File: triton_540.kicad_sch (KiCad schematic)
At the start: 24 parts, among them J1 REC ANT, SW1 Band Switch B

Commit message: first draft of vfo sheet
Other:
- added sheet VFO-80289 (VFO_80289.kicad_sch)
- note added: "VFO 80289"
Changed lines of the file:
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@@
 		(title "Ten Tec Triton IV Model 540 Transceiver")
 		(date "2026-07-26")
-		(rev "0.1")
+		(rev "0.2")
 		(company "Andy McCann KA3KAF & DOug McCann KA3KAG")
 	)
@@
 		)
 	)
+	(text "VFO\n80289"
+		(exclude_from_sim no)
+		(at 166.116 122.174 0)
+		(effects
+			(font
+				(size 2.54 2.54)
+			)
+		)
+	)
 	(junction
 		(at 123.19 80.01)
@@
 				)
 			)
+		)
+	)
+	(sheet
+		(at 146.05 110.49)
+		(size 40.64 22.86)
+		(exclude_from_sim no)
+		(in_bom yes)
+		(on_board yes)
+		(dnp no)
+		(fields_autoplaced yes)
+		(stroke
+			(width 0.1524)
+			(type solid)
+		)
+		(fill
+			(color 0 0 0 0)
+		)
+		(property "Sheetname" "VFO-80289"
+			(at 146.05 109.7784 0)
+			(hide yes)
+			(show_name no)
+			(do_not_autoplace no)
+			(effects
+				(font
+					(size 1.27 1.27)
+				)
+				(justify left bottom)
+			)
+		)
+		(property "Sheetfile" "VFO_80289.kicad_sch"
+			(at 146.05 133.9346 0)
+			(hide yes)
+			(show_name no)
+			(do_not_autoplace no)
+			(effects
+				(font
+					(size 1.27 1.27)
+				)
+				(justify left top)
+			)
+		)
+		(pin "+12" input
+			(at 151.13 110.49 90)
+			(effects
+				(font
+					(size 1.27 1.27)
+				)
+				(justify right)
+			)
+		)
+		(pin "+REG" input
+			(at 166.37 110.49 90)
+			(effects
+				(font
+					(size 1.27 1.27)
+				)
+				(justify right)
+			)
+		)
+		(pin "OFFSET" input
+			(at 179.07 133.35 270)
+			(effects
+				(font
+					(size 1.27 1.27)
+				)
+				(justify left)
+			)
+		)
+		(pin "OUT" input
+			(at 186.69 115.57 0)
+			(effects
+				(font
+					(size 1.27 1.27)
+				)
+				(justify right)
+			)
+		)
+		(pin "S5" input
+			(at 166.37 133.35 270)
+			(effects
+				(font
+					(size 1.27 1.27)
+				)
+				(justify left)
+			)
+		)
+		(instances
+			(project "triton_540"
+				(path "/2d45daab-5f60-4e97-8c02-32b0054eab28"
+					(page "3")
+				)
+			)

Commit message: Release VFO 80289 and mixer 80287 v0.2.0
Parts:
- removed C66-10: 5p, symbol Device:C_Small_US
- removed C99: .01u, symbol Device:C_Small_US
- removed R66-8: 1Meg, symbol Device:R_Small_US
- removed R98: 50, symbol Device:R_Small_US
- removed R99: 1Gig, symbol Device:R_Small_US
- removed V1: 12, symbol Simulation_SPICE:VDC
- removed V2: 3.9, symbol Simulation_SPICE:VDC
- removed V3: 0, symbol Simulation_SPICE:VDC
- added C21: 560p, symbol Device:C_Small_US
- added S5: 10M Band Switch, symbol triton_iv:SW_Rotary_1x4
- added Y1: 13.99MHz, symbol Device:Crystal_Small
- added Y2: 14.49MHz, symbol Device:Crystal_Small
- added Y3: 14.99MHz, symbol Device:Crystal_Small
- added Y4: 15.49MHz, symbol Device:Crystal_Small
- renumbered SW1 to S4B1
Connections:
- net RF_Amp_80166/S4B: now also S4B1.12 (Pole-B); no longer S4B1.6
- net VFO-80289/S5: now also S5.5 (Pole-A)
- net at C17.1, C18.1: now also S4B1.8 (40M-B); no longer S4B1.2
- net at C16.1: now also S4B1.9 (20M-B); no longer S4B1.3
- net at C13.1: now also S4B1.11 (10M-B); no longer S4B1.5
- net at C19.1, C20.1: now also S4B1.7 (80M-B); no longer S4B1.1
- net at C15.1: now also S4B1.10 (15M-B); no longer S4B1.4
- new net: S5.2 (40M-A), Y2.1
- new net: S5.4 (10M-A), Y4.1
- new net: S5.1 (80M-A), Y1.1
- new net: S5.3 (10M-A), Y3.1
- new net VFO-80289/GND: C21.1, C21.2, Y1.2, Y2.2, Y3.2, Y4.2
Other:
- added sheet TX RX Mixer 80287 (tx_rx_mixer_80287.kicad_sch)
- sheet VFO-80289 ports: added GND; removed none
- note added: ".param S4_POS=1 .param S5_POS=1"
- note added: ".tran 2n 100u 60u 2n"
- note added: "28.0"
- note added: "28.5"
- note added: "29.0"
- note added: "TX RX MIXER 80287"
- note removed: ".option rshunt=1e12"
- note removed: ".param S4_POS=5 .param L_RACK=1.4253u .param L2_TRACK=0.0849053 .param L2_OFFSET=1.97963u .ac dec 10000 28.8Meg 29.2Meg"
- note removed: "L_RACK represents the RESONATE-control position."
- note removed: "Sim only"

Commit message: updates to topsheet
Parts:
- added J2: (no value), symbol triton_iv:Octal_Plug
- added S2: TR-R, symbol Switch:SW_SPST
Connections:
- net TX RX Mixer 80287/Rx VFO : now also J2. (7)
- net TX RX Mixer 80287/Tx VFO: now also J2. (7)
- net VFO-80289/+12: now also J2. (7)
- net VFO-80289/GND: no longer C21.1, Y1.2, Y2.2, Y3.2, Y4.2
- net VFO-80289/OUT: now also J2. (7)
- net RF_Amp_80166/ANT renamed RCV2
- net RCV2: now also S2.1 (A)
- new net: C21.1, Y1.2, Y2.2, Y3.2, Y4.2
- new net RCV1: S2.2 (B)
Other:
- added sheet IF-AGC_80279 (if-agc_80279.kicad_sch)
- note added: "IF-AGC 80279"
- moved on the sheet: C10, C11, C12, C8, C9, S4A

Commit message: work on if-agc
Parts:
- added C3: 1000m, symbol Device:C_Polarized_Small_US
- added D1: D, symbol Device:D
- added F1: Fuse_Small, symbol Device:Fuse_Small
- added J3: Conn_01x04, symbol Connector_Generic:Conn_01x04
- added L1: L, symbol Device:L
- added LA1, LA2: 120, symbol Device:Lamp
- added LA3: ${SIM.PARAMS}, symbol Device:Lamp
- added LA4: 144, symbol Device:Lamp
- added R1: 150, symbol Device:R_Small_US
- added R2: 47, symbol Device:R_Small_US
- added S1: TR-R, symbol Switch:SW_SPST
- added V1: 13.28, symbol Simulation_SPICE:VDC
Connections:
- net VFO-80289/+12 is gone; now on net VFO-80289/OUT: J2. (7)
- net GND: now also C3.2, D1.2 (A), J3.1 (Pin_1), LA1.1 (-), LA3.1 (-), LA4.2 (+), V1.2
- new net: J3.2 (Pin_2), S1.1 (A)
- new net: J3.3 (Pin_3), S1.2 (B)
- new net: LA1.2 (+), R1.2
- new net: LA2.1 (-), LA3.2 (+)
- new net: LA4.1 (-), R2.2
- new net +12: C3.1, J2. (7), L1.2, LA2.2 (+), R1.1, R2.1
- new net +13.28: F1.2, J3.4 (Pin_4), V1.1
- new net L1: D1.1 (K), F1.1, L1.1
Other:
- note added: "FUSE AGC 20"
- note added: "PWR SW Located on AG Control"

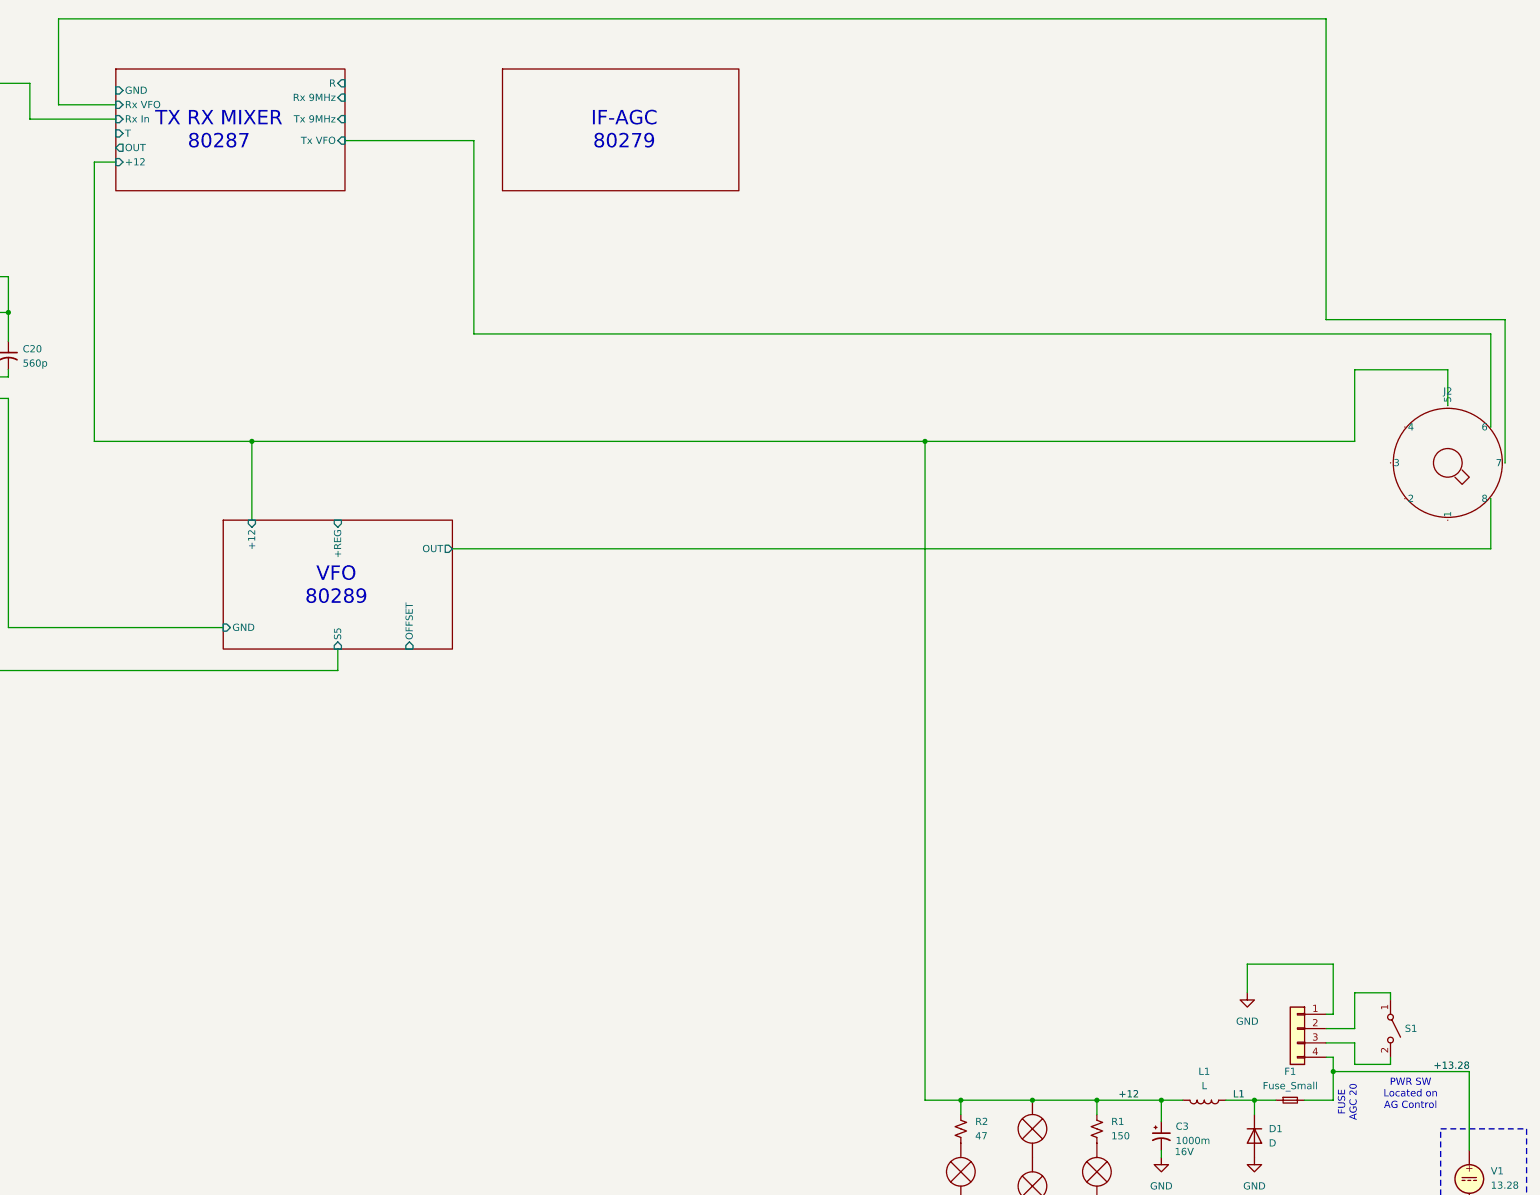
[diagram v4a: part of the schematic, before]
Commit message: Add TX-RX mixer simulations
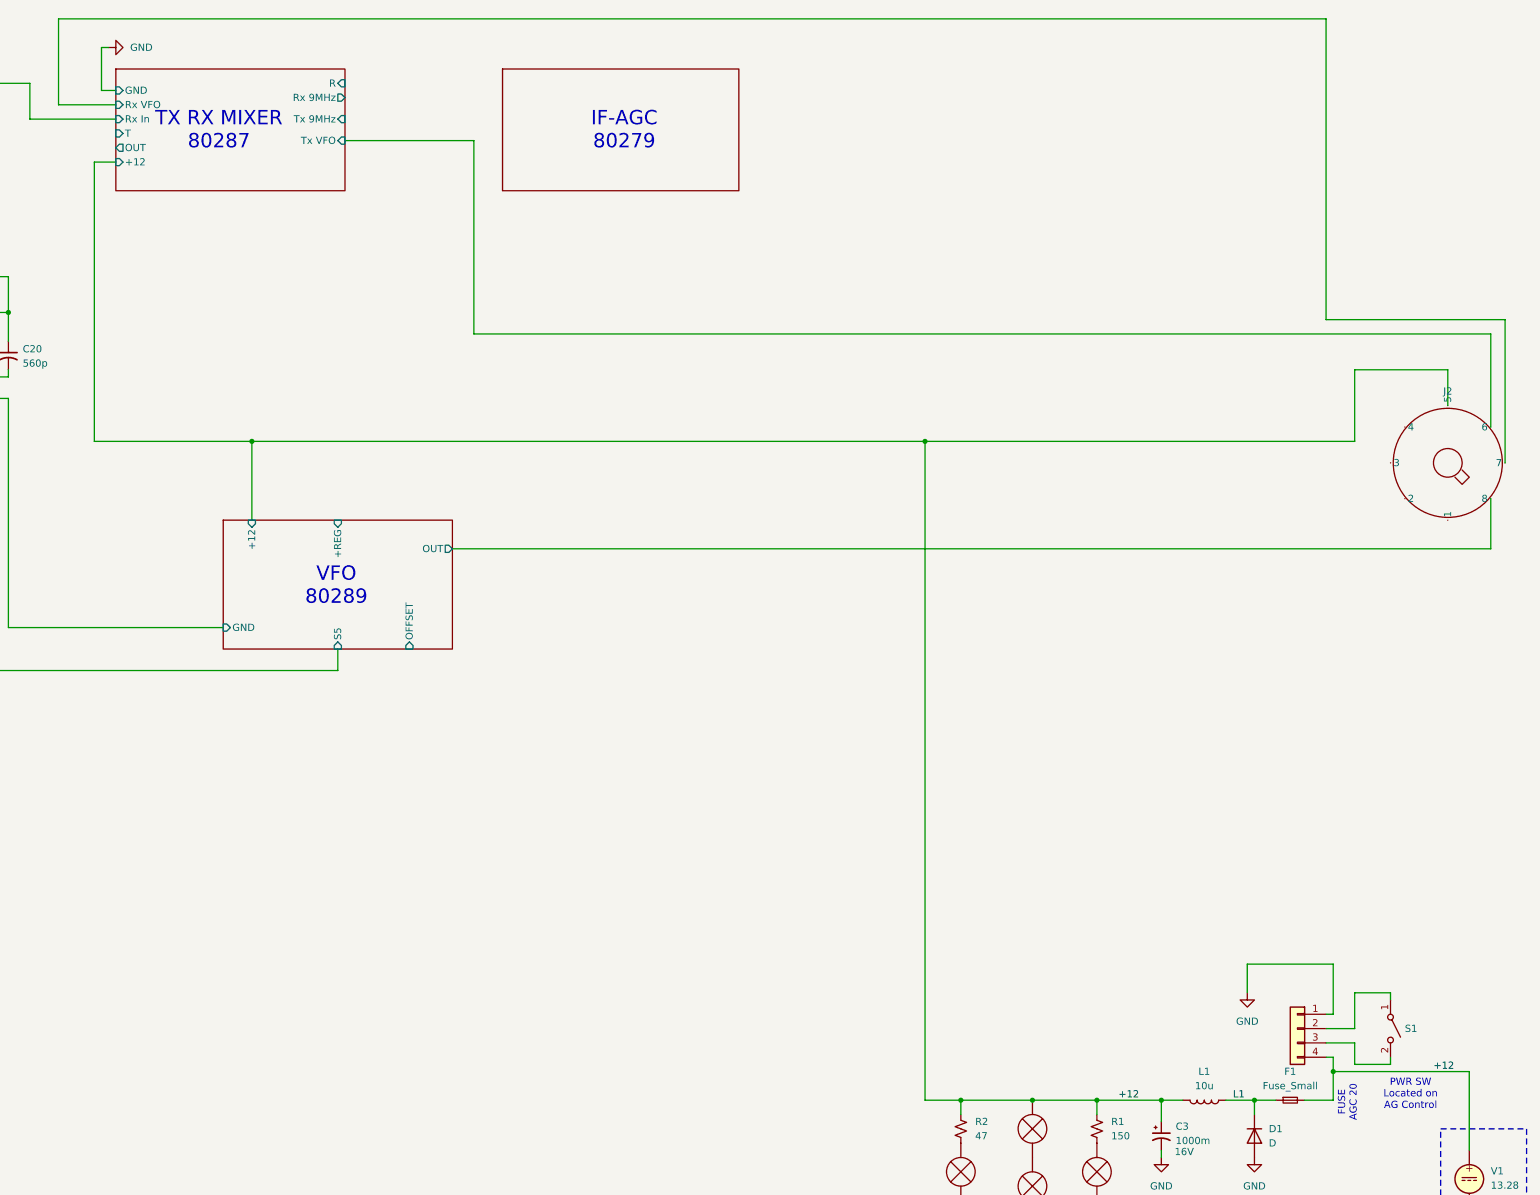
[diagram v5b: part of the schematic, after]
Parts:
- L1: value L -> 10u
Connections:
- net +13.28 is gone; now on net +12: F1.2, J3.4 (Pin_4), V1.1
- net TX RX Mixer 80287/Rx VFO  is gone; now on net VFO-80289/OUT: J2. (7)
- new net TX RX Mixer 80287/Rx VFO: J2. (7)
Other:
- sheet TX RX Mixer 80287 ports: added Rx VFO; removed Rx VFO 
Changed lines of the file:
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@@
 	(wire
 		(pts
+			(xy 167.64 29.21) (xy 165.1 29.21)
+		)
+		(stroke
+			(width 0)
+			(type default)
+		)
+	)
+	(wire
+		(pts
 			(xy 48.26 63.5) (xy 48.26 64.77)
 		)
@@
 	(wire
 		(pts
+			(xy 165.1 29.21) (xy 165.1 21.59)
+		)
+		(stroke
+			(width 0)
+			(type default)
+		)
+	)
+	(wire
+		(pts
 			(xy 383.54 200.66) (xy 383.54 203.2)
 		)
@@
 	(wire
 		(pts
+			(xy 165.1 21.59) (xy 166.37 21.59)
+		)
+		(stroke
+			(width 0)
+			(type default)
+		)
+	)
+	(wire
+		(pts
 			(xy 167.64 31.75) (xy 157.48 31.75)
 		)
@@
 		)
 	)
-	(label "+13.28"
+	(label "+12"
 		(at 401.32 203.2 0)
 		(effects
@@
 		(unit 1)
 		(body_style 1)
-		(exclude_from_sim no)
+		(exclude_from_sim yes)
 		(in_bom yes)
 		(on_board yes)
@@
 		(unit 1)
 		(body_style 1)
-		(exclude_from_sim no)
+		(exclude_from_sim yes)
 		(in_bom yes)
 		(on_board yes)
@@
 	)
 	(symbol
+		(lib_id "power:GND")
+		(at 166.37 21.59 90)
+		(unit 1)
+		(body_style 1)
+		(exclude_from_sim no)
+		(in_bom yes)
+		(on_board yes)
+		(in_pos_files yes)
+		(dnp no)
+		(fields_autoplaced yes)
+		(property "Reference" "#PWR099"
+			(at 172.72 21.59 0)
+			(hide yes)
+			(show_name no)
+			(do_not_autoplace no)
+			(effects
+				(font
+					(size 1.27 1.27)
+				)
+			)
+		)
+		(property "Value" "GND"
+			(at 170.18 21.5899 90)
+			(show_name no)
+			(do_not_autoplace no)
+			(effects
+				(font
+					(size 1.27 1.27)
+				)
+				(justify right)
+			)
+		)
+		(property "Footprint" ""
+			(at 166.37 21.59 0)
+			(hide yes)
+			(show_name no)
+			(do_not_autoplace no)
+			(effects
+				(font
+					(size 1.27 1.27)
+				)
+			)
+		)
+		(property "Datasheet" ""
+			(at 166.37 21.59 0)
+			(hide yes)
+			(show_name no)
+			(do_not_autoplace no)
+			(effects
+				(font
+					(size 1.27 1.27)
+				)
+			)
+		)
+		(property "Description" "Power symbol creates a global label with name \"GND\" , ground"
+			(at 166.37 21.59 0)
+			(hide yes)
+			(show_name no)
+			(do_not_autoplace no)
+			(effects
+				(font
+					(size 1.27 1.27)
+				)
+			)
+		)
+		(pin "1"
+		)
+		(instances
+			(project "triton_540"
+				(path "/2d45daab-5f60-4e97-8c02-32b0054eab28"
+					(reference "#PWR099")
+					(unit 1)
+				)
+			)
+		)
+	)
+	(symbol
 		(lib_id "Device:C_Small_US")
 		(at 63.5 67.31 0)
@@
 			)
 		)
-		(property "Value" "L"
+		(property "Value" "10u"
 			(at 360.68 205.74 90)
 			(show_name no)
@@
 		(unit 1)
 		(body_style 1)
-		(exclude_from_sim no)
+		(exclude_from_sim yes)
 		(in_bom yes)
 		(on_board yes)
@@
 		(unit 1)
 		(body_style 1)
-		(exclude_from_sim no)
+		(exclude_from_sim yes)
 		(in_bom yes)
 		(on_board yes)
@@
 		(at 186.69 105.41)
 		(size 40.64 22.86)
-		(exclude_from_sim no)
+		(exclude_from_sim yes)
 		(in_bom yes)
 		(on_board yes)
@@
 		(at 167.64 25.4)
 		(size 40.64 21.59)
-		(exclude_from_sim yes)
+		(exclude_from_sim no)
 		(in_bom yes)
 		(on_board yes)
@@
 			)
 		)
-		(pin "Rx 9MHz" input
+		(pin "Rx 9MHz" output
 			(at 208.28 30.48 0)
 			(effects
@@
 			)
 		)
-		(pin "Rx VFO " input
+		(pin "Rx VFO" input
 			(at 167.64 31.75 180)
 			(effects

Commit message: Complete IF-AGC schematic and SPICE models
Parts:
- added C8: .01u, symbol Device:C_Small_US
- added J4: AUX 12V, symbol Connector:Conn_Coaxial
- added J5: KEY, symbol Connector:Conn_Coaxial
- added J6: PTT, symbol Connector:Conn_Coaxial
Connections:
- net +12: now also J4.1 (In)
- net GND: now also C8.2, J4.2 (Ext), J5.2 (Ext), J6.2 (Ext)
- new net: C8.1, J6.1 (In)
- no-connect marks 0 -> 1
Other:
- company: Andy McCann KA3KAF & DOug McCann KA3KAG -> Andy McCann KA3KAF & Doug McCann KA3KAG
